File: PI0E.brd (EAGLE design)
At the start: 36 parts, among them IC1 ENC28J60QFN, T1 WE-LAN-10/100/1000-BASE-T,749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, U1 TPS73533DRVR, U2 CAT24C32WI-GT3, X1 22-23-2021, X2 22-23-2021

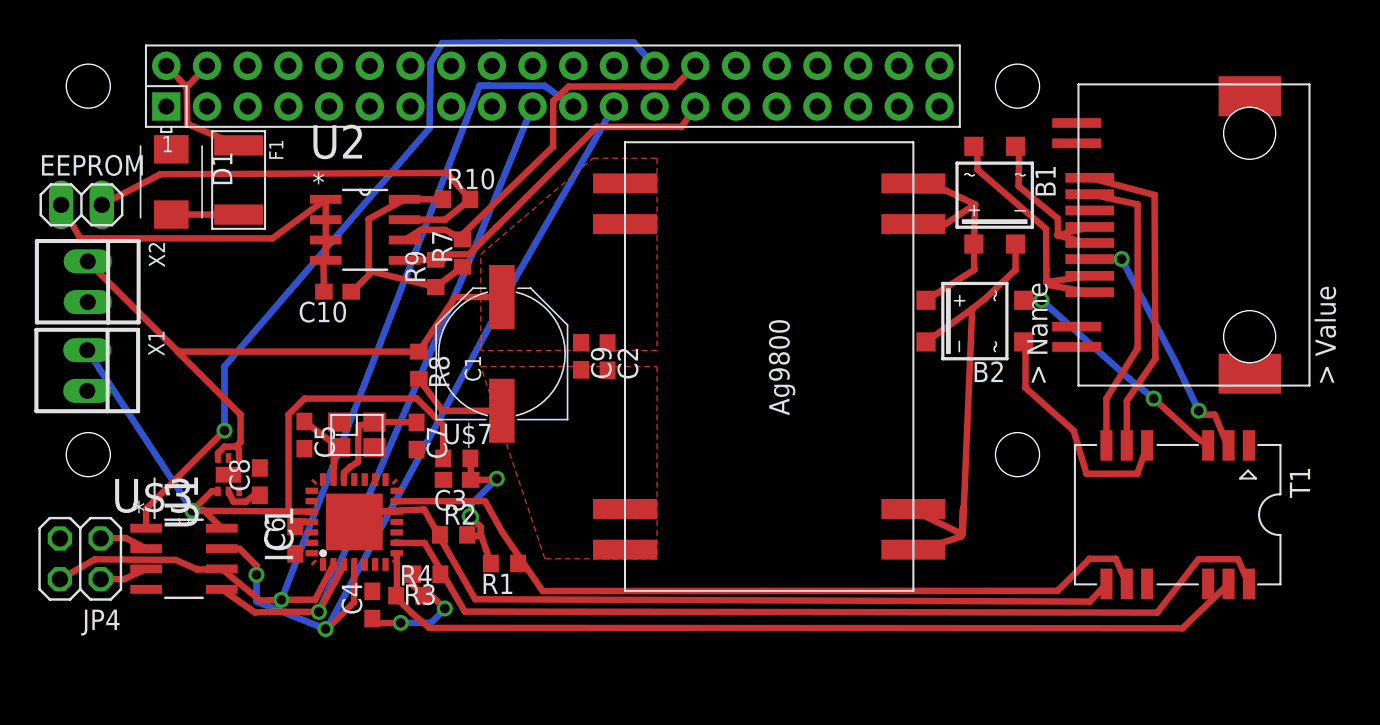
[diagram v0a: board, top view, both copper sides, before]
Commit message: Cleaning up routing
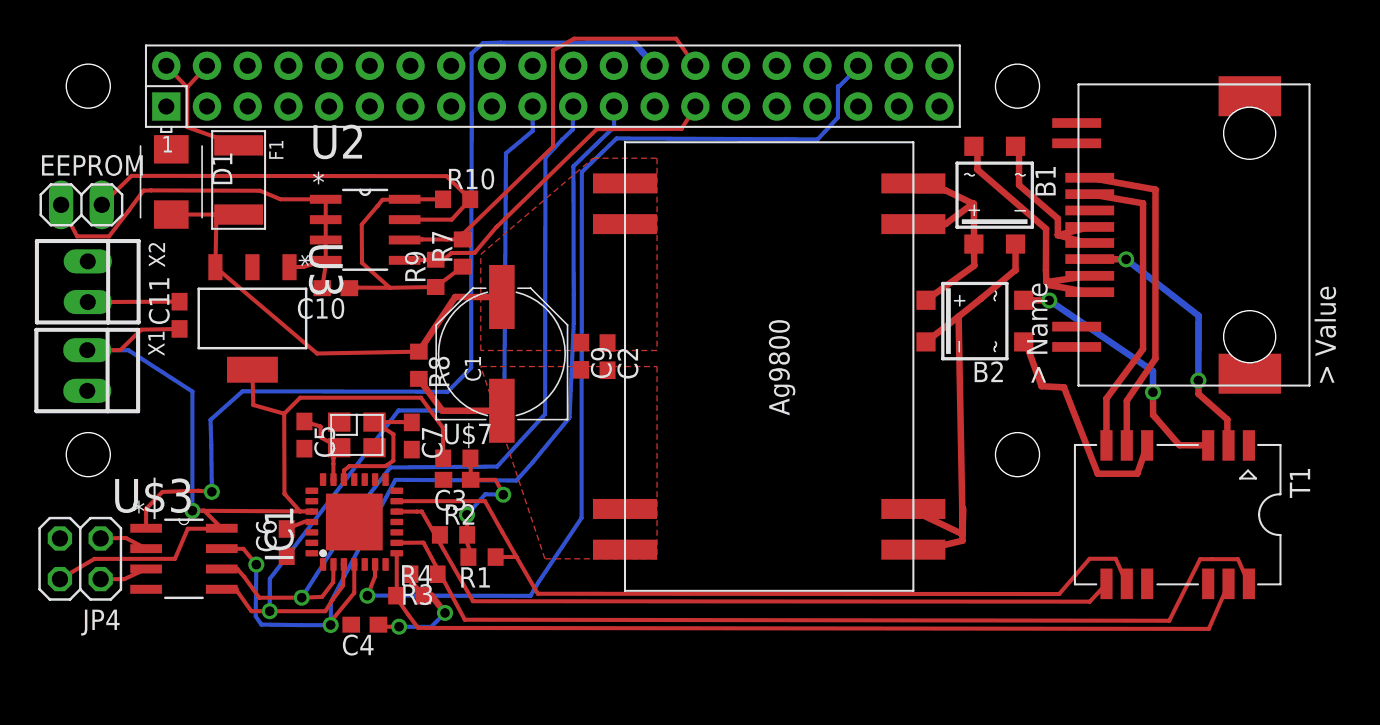
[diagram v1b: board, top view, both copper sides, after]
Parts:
- removed C8: .01uF, rcl:C0603
- removed U1: TPS73533DRVR, Texas Instruments_By_element14_Batch_1:SON65P200X200X80-7N
- added C11: 100uF, rcl:C0603
- added U3: TLV1117-33CDCY, Texas Instruments_By_element14_Batch_1:SOT230P700X180-4N
- moved R1 1.46 mm to (28.1, 7.11)
- moved C4 1.32 mm to (20.8, 2.89), turned to 180 degrees
- moved C6 0.55 mm to (15.9, 8.01)
- moved C7 0.30 mm to (23.7, 14.7)
- moved C10 0.25 mm to (18.9, 23.9)
- moved R3 0.17 mm to (24.5, 6.04)
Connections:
- removed net N$20: C8.1, U1.2
- net !RESET: now also U$1.36
- net +3V3: now also C11.1, IC1.21, U3.4; no longer U1.1
- net +5V: now also U3.3; no longer U1.4, U1.6
- net GND: now also C11.2, IC1.18, U3.1; no longer C8.2, U1.3
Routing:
- net !RESET: track 0.00 -> 60.8 mm
- net +5V: track 44.3 -> 29.2 mm
- net +3V3: track 69.5 -> 84.5 mm
- net !CS2: track 51.2 -> 59.8 mm
- net GND: track 30.5 -> 39.1 mm
- net SI: track 44.1 -> 52.0 mm
- net SCK: track 51.6 -> 58.4 mm
- net TX-: track 51.5 -> 48.0 mm
- net ID_SC: track 24.7 -> 27.8 mm
- net N$20: track 2.50 -> 0.00 mm
- net TX+: track 50.5 -> 52.3 mm
- net N$8: track 7.47 -> 9.23 mm
- net N$7: track 14.9 -> 16.5 mm
- net 6: track 15.9 -> 17.0 mm
- net RX+: track 58.5 -> 59.6 mm
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
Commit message: updated drill sizes
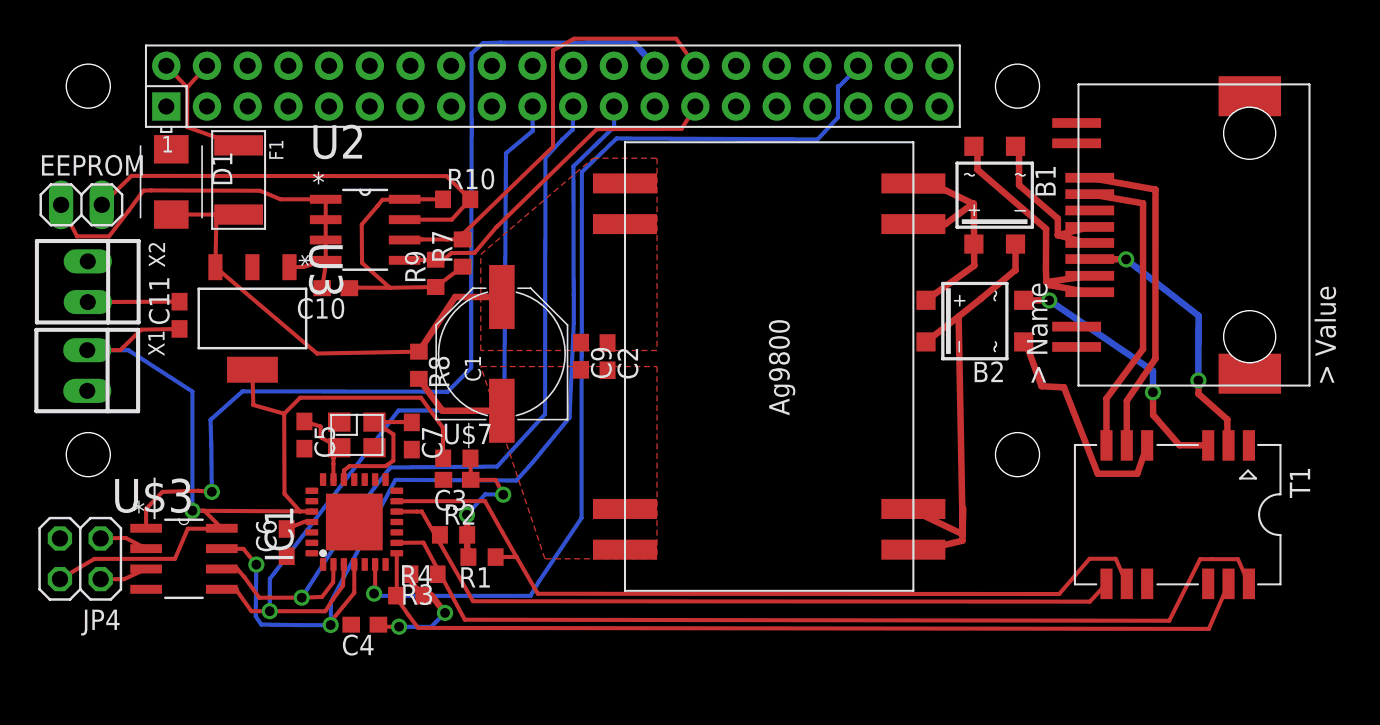
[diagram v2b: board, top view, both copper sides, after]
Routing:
- net !RESET: track 60.8 -> 60.3 mm, vias 0 -> 1
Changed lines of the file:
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@@
 <?xml version="1.0" encoding="utf-8"?>
 <!DOCTYPE eagle SYSTEM "eagle.dtd">
-<eagle version="7.5.0">
+<eagle version="6.5.0">
 <drawing>
 <settings>
@@
 <pass name="Default">
 <param name="RoutingGrid" value="50mil"/>
-<param name="AutoGrid" value="1"/>
-<param name="Efforts" value="0"/>
-<param name="TopRouterVariant" value="1"/>
 <param name="tpViaShape" value="round"/>
 <param name="PrefDir.1" value="|"/>
@@
 <wire x1="72.789" y1="18.128" x2="72.8" y2="22.174" width="0.4064" layer="16"/>
 <wire x1="72.8" y1="22.174" x2="68.281" y2="25.689" width="0.4064" layer="16"/>
-<via x="68.281" y="25.689" extent="1-16" drill="0.6"/>
-<via x="72.789" y="18.128" extent="1-16" drill="0.6"/>
+<via x="68.281" y="25.689" extent="1-16" drill="0.6096"/>
+<via x="72.789" y="18.128" extent="1-16" drill="0.6096"/>
 </signal>
 <signal name="+5V">
@@
 <wire x1="22.86" y1="16.256" x2="14.83" y2="5.741" width="0.254" layer="16"/>
 <wire x1="14.83" y1="5.741" x2="14.825" y2="3.729" width="0.254" layer="16"/>
-<via x="14.825" y="3.729" extent="1-16" drill="0.6"/>
+<via x="14.825" y="3.729" extent="1-16" drill="0.6096"/>
 <contactref element="IC1" pad="3"/>
 <wire x1="19.455" y1="6.645" x2="19.448" y2="6.645" width="0.4064" layer="1"/>
@@
 <wire x1="22.352" y1="12.7" x2="20.574" y2="10.414" width="0.254" layer="16"/>
 <wire x1="20.574" y1="10.414" x2="16.822" y2="4.572" width="0.254" layer="16"/>
-<via x="16.822" y="4.572" extent="1-16" drill="0.6"/>
+<via x="16.822" y="4.572" extent="1-16" drill="0.6096"/>
 <contactref element="IC1" pad="2"/>
 <wire x1="18.811" y1="6.646" x2="18.805" y2="6.645" width="0" layer="19" extent="1-1"/>
@@
 <wire x1="22.668" y1="11.926" x2="18.642" y2="4.314" width="0.254" layer="16"/>
 <wire x1="18.642" y1="4.314" x2="18.639" y2="2.868" width="0.254" layer="16"/>
-<via x="13.99" y="6.637" extent="1-16" drill="0.6"/>
+<via x="13.99" y="6.637" extent="1-16" drill="0.6096"/>
 <wire x1="13.99" y1="6.637" x2="13.179" y2="7.622" width="0.254" layer="1"/>
 <wire x1="13.179" y1="7.622" x2="11.8462" y2="7.622" width="0.254" layer="1"/>
@@
 <wire x1="14.302" y1="2.894" x2="16.802" y2="2.858" width="0.254" layer="16"/>
 <wire x1="16.802" y1="2.858" x2="18.661" y2="2.858" width="0.254" layer="16"/>
-<via x="18.629" y="2.868" extent="1-16" drill="0.6"/>
+<via x="18.629" y="2.868" extent="1-16" drill="0.6096"/>
 <contactref element="IC1" pad="4"/>
 <wire x1="20.105" y1="6.645" x2="20.103" y2="6.645" width="0.4064" layer="1"/>
@@
 <wire x1="18.579" y1="3.003" x2="18.629" y2="2.868" width="0.254" layer="1"/>
 <wire x1="18.629" y1="2.868" x2="18.639" y2="2.868" width="0" layer="19" extent="16-16"/>
-<wire x1="18.661" y1="2.858" x2="18.579" y2="3.003" width="0" layer="19" extent="1-16"/>
+<wire x1="18.661" y1="2.858" x2="18.639" y2="2.868" width="0" layer="19" extent="16-16"/>
 </signal>
 <signal name="GND">
@@
 <wire x1="34.253" y1="18.793" x2="29.314" y2="16.239" width="0" layer="19" extent="1-1"/>
 <wire x1="35.912" y1="18.769" x2="34.253" y2="18.793" width="0" layer="19" extent="1-1"/>
-<wire x1="19.909" y1="2.886" x2="17.455" y2="8.645" width="0" layer="19" extent="1-1"/>
+<wire x1="19.909" y1="2.886" x2="15.885" y2="7.16" width="0" layer="19" extent="1-1"/>
 <wire x1="37" y1="10.11" x2="35.912" y2="18.769" width="0" layer="19" extent="1-1"/>
 <wire x1="7.1088" y1="5.095" x2="15.885" y2="7.16" width="0" layer="19" extent="1-1"/>
@@
 <wire x1="69.954" y1="17.393" x2="69.956" y2="18.718" width="0.4064" layer="16"/>
 <wire x1="69.956" y1="18.718" x2="63.483" y2="23.124" width="0.4064" layer="16"/>
-<via x="63.483" y="23.124" extent="1-16" drill="0.6"/>
-<via x="69.954" y="17.393" extent="1-16" drill="0.6"/>
+<via x="63.483" y="23.124" extent="1-16" drill="0.6096"/>
+<via x="69.954" y="17.393" extent="1-16" drill="0.6096"/>
 </signal>
 <signal name="N$9">
@@
 <contactref element="R2" pad="2"/>
 <contactref element="U$7" pad="2"/>
-<wire x1="27.149" y1="8.491" x2="27.125" y2="8.406" width="0.4064" layer="1"/>
-<wire x1="27.125" y1="8.406" x2="27.044" y2="8.29" width="0.254" layer="1"/>
-<wire x1="27.044" y1="8.29" x2="27.33" y2="7.463" width="0.254" layer="1"/>
 <wire x1="27.33" y1="7.463" x2="27.225" y2="7.106" width="0.254" layer="1"/>
-<wire x1="27.125" y1="8.406" x2="27.125" y2="8.99" width="0.254" layer="1"/>
-<wire x1="27.125" y1="8.99" x2="27.137" y2="9.748" width="0.254" layer="1"/>
 <wire x1="27.137" y1="9.748" x2="28.276" y2="11.028" width="0.254" layer="16"/>
 <wire x1="28.276" y1="11.028" x2="29.4" y2="11" width="0.254" layer="16"/>
-<via x="27.137" y="9.748" extent="1-16" drill="0.6"/>
+<via x="27.137" y="9.748" extent="1-16" drill="0.6096"/>
 <wire x1="27.37" y1="11.928" x2="28.928" y2="11.928" width="0.254" layer="1"/>
 <wire x1="28.928" y1="11.928" x2="29.4" y2="11" width="0.254" layer="1"/>
 <wire x1="27.37" y1="11.928" x2="27.37" y2="13.251" width="0.254" layer="1"/>
 <wire x1="27.37" y1="13.251" x2="27.352" y2="13.269" width="0.4064" layer="1"/>
-<via x="29.4" y="11" extent="1-16" drill="0.6"/>
+<via x="29.4" y="11" extent="1-16" drill="0.6096"/>
+<wire x1="27.33" y1="7.463" x2="27.149" y2="7.463" width="0.4064" layer="1"/>
+<wire x1="27.149" y1="7.463" x2="27.149" y2="8.491" width="0.4064" layer="1"/>
+<wire x1="27.149" y1="8.491" x2="27.137" y2="8.491" width="0.4064" layer="1"/>
+<wire x1="27.137" y1="8.491" x2="27.137" y2="9.748" width="0.4064" layer="1"/>
 </signal>
 <signal name="+3V3">
@@
 <wire x1="6" y1="20.021" x2="10.003" y2="17.436" width="0.254" layer="16"/>
 <wire x1="10.003" y1="17.436" x2="10" y2="10" width="0.254" layer="16"/>
-<via x="10" y="10" extent="1-16" drill="0.6"/>
+<via x="10" y="10" extent="1-16" drill="0.6096"/>
 <wire x1="16.719684375" y1="9.956540625" x2="10" y2="10" width="0.254" layer="1"/>
 <wire x1="25.184" y1="23.965" x2="26.861" y2="25.233" width="0.254" layer="1"/>
@@
 <wire x1="5.5" y1="20.021" x2="3.435" y2="20.021" width="0.254" layer="1"/>
 <wire x1="24.264" y1="17.055" x2="25.184" y2="23.965" width="0" layer="19" extent="1-1"/>
+<wire x1="11.9642" y1="8.875" x2="11.8332" y2="8.905" width="0" layer="19" extent="1-1"/>
 <wire x1="18.155" y1="11.945" x2="17.455" y2="9.945" width="0" layer="19" extent="1-1"/>
-<wire x1="11.9642" y1="8.875" x2="11.8332" y2="8.905" width="0" layer="19" extent="1-1"/>
 </signal>
 <signal name="N$18">
@@
 <wire x1="24.415" y1="4.698" x2="24.932" y2="4.698" width="0.4064" layer="1"/>
 <wire x1="24.932" y1="4.698" x2="25.763" y2="3.613" width="0.4064" layer="1"/>
-<via x="25.766" y="3.622" extent="1-16" drill="0.6"/>
-<via x="22.9" y="2.76" extent="1-16" drill="0.6"/>
+<via x="25.766" y="3.622" extent="1-16" drill="0.6096"/>
+<via x="22.9" y="2.76" extent="1-16" drill="0.6096"/>
 <wire x1="25.763" y1="3.613" x2="25.766" y2="3.622" width="0" layer="19" extent="1-1"/>
 <wire x1="25.763" y1="3.613" x2="25.763" y2="3.613" width="0" layer="19" extent="1-16"/>
@@
 <wire x1="8.128" y1="11.176" x2="10.376" y2="11.246" width="0.254" layer="1"/>
 <wire x1="10.376" y1="11.246" x2="11.212" y2="11.178" width="0.254" layer="1"/>
-<via x="11.212" y="11.178" extent="1-16" drill="0.6"/>
+<via x="11.212" y="11.178" extent="1-16" drill="0.6096"/>
 <wire x1="11.212" y1="11.178" x2="11.176" y2="14.124" width="0.254" layer="16"/>
 <wire x1="11.176" y1="14.124" x2="11.13" y2="15.676" width="0.254" layer="16"/>
@@
 <contactref element="U$1" pad="36"/>
 <contactref element="IC1" pad="6"/>
-<wire x1="21.405" y1="6.645" x2="21.395" y2="5.885" width="0.254" layer="1"/>
-<wire x1="21.395" y1="5.885" x2="20.924" y2="4.706" width="0.254" layer="1"/>
 <wire x1="51.55" y1="37.77" x2="51.55" y2="37.673" width="0.4064" layer="16"/>
 <wire x1="51.55" y1="37.673" x2="50.377" y2="36.5" width="0.254" layer="16"/>
@@
 <wire x1="34.288" y1="9.548" x2="31.62" y2="5.57" width="0.254" layer="16"/>
 <wire x1="31.62" y1="5.57" x2="31.1" y2="4.684" width="0.254" layer="16"/>
-<wire x1="31.1" y1="4.684" x2="20.924" y2="4.706" width="0.254" layer="16"/>
 <wire x1="50.377" y1="36.5" x2="50.292" y2="36.5" width="0.254" layer="16"/>
 <wire x1="50.292" y1="36.5" x2="50.292" y2="34.544" width="0.254" layer="16"/>
 <wire x1="50.292" y1="34.544" x2="49.022" y2="33.174" width="0.254" layer="16"/>
 <wire x1="49.022" y1="33.174" x2="46.974" y2="33.187" width="0.254" layer="16"/>
-<wire x1="20.924" y1="4.706" x2="20.924" y2="4.706" width="0" layer="19" extent="1-16"/>
+<wire x1="31.1" y1="4.684" x2="21.478" y2="4.684" width="0.254" layer="16"/>
+<wire x1="21.478" y1="4.684" x2="21.336" y2="4.826" width="0.254" layer="16"/>
+<via x="21.336" y="4.826" extent="1-16" drill="0.6096"/>
+<wire x1="21.405" y1="6.645" x2="21.405" y2="4.895" width="0.254" layer="1"/>
+<wire x1="21.405" y1="4.895" x2="21.336" y2="4.826" width="0.254" layer="1"/>
 </signal>
 <signal name="N$15">
@@
 <contactref element="IC1" pad="28"/>
 </signal>
-<signal name="N$19">
-<via x="20.924" y="4.696" extent="1-16" drill="0.6"/>
-</signal>
 </signals>

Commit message: Laid ground plane
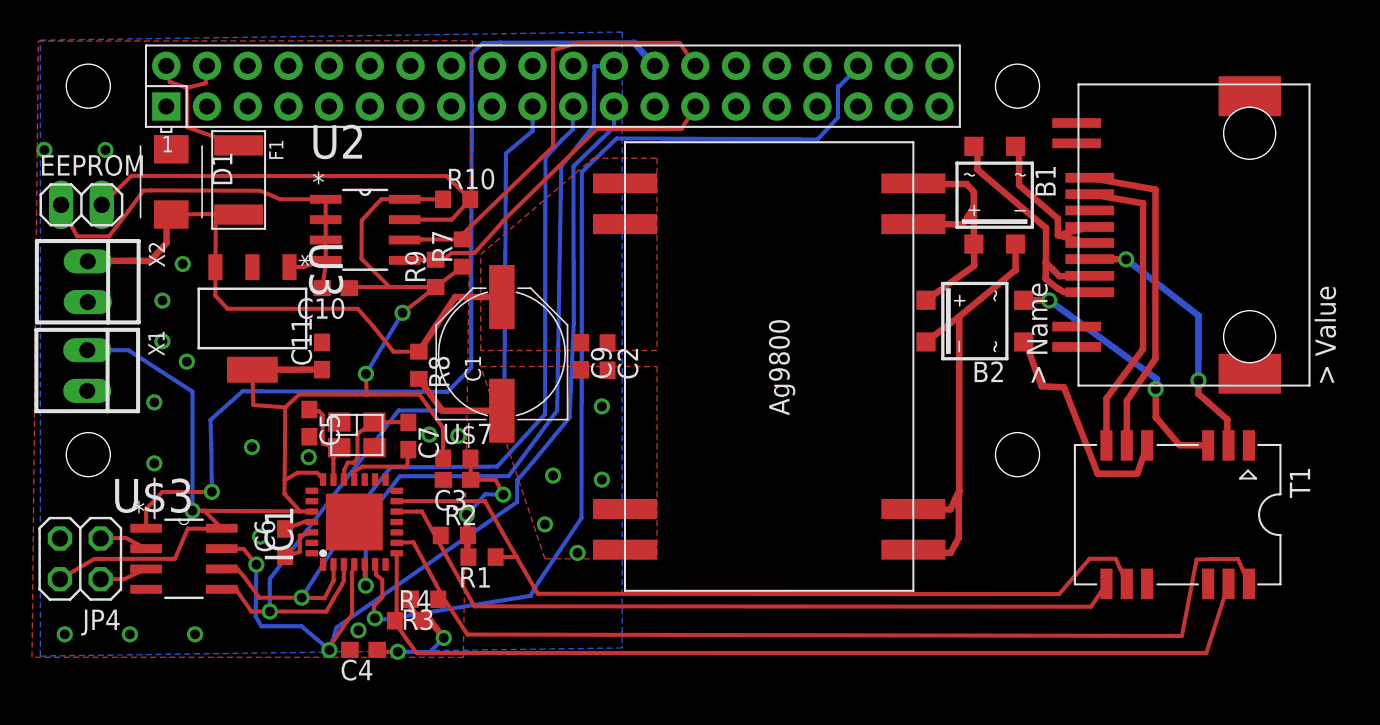
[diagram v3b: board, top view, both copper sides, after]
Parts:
- moved C11 9.25 mm to (18.1, 19.7)
- moved R4 1.57 mm to (23.5, 3.13)
- moved C4 1.57 mm to (20.7, 1.32)
- moved R3 1.57 mm to (24.5, 4.47)
- moved C5 0.80 mm to (17.3, 15.5)
- moved C7 0.22 mm to (23.5, 14.7)
- moved C6 0.10 mm to (15.8, 8.01)
- moved R2 0.06 mm to (26.3, 8.46)
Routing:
- net !CS: track 0.00 -> 44.3 mm, vias 0 -> 1
- net +3V3: track 84.5 -> 94.0 mm, vias 1 -> 3
- net +5V: track 29.2 -> 38.1 mm
- net VIN+: track 32.8 -> 29.9 mm
- net RX-: track 57.5 -> 60.5 mm
- net N$8: track 9.23 -> 6.81 mm
- net RX+: track 59.6 -> 61.9 mm
- net GND: track 39.1 -> 41.1 mm, vias 0 -> 15
- net !RESET: track 60.3 -> 62.3 mm
- net VIN-: track 15.7 -> 16.7 mm
- net SCK: track 58.4 -> 59.4 mm
- net N$10: track 5.47 -> 6.21 mm
- net 5V0@1: track 9.59 -> 10.3 mm
- net N$14: track 1.22 -> 1.75 mm
- net TX-: track 48.0 -> 48.5 mm
- added copper zone on layer 1, net +5V
- added copper zone on layer 1, net GND
- added copper zone on layer 16, net GND
- removed copper zone on layer 1, net N$34
- removed copper zone on layer 1, net N$35

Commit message: No more air wires
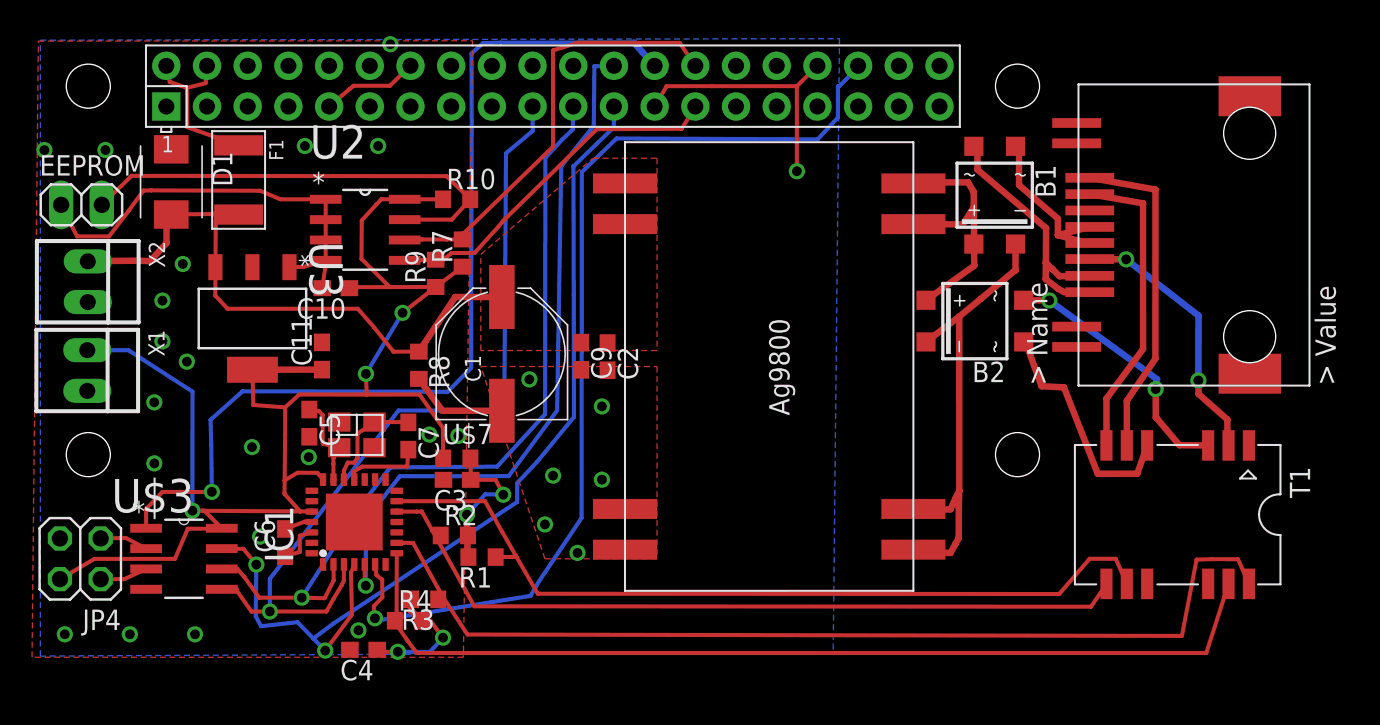
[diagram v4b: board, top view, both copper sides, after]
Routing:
- net GND: track 41.1 -> 63.9 mm, vias 15 -> 26
- net TX-: track 48.5 -> 49.2 mm
